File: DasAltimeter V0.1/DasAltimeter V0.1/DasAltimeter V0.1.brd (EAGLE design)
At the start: 39.6 x 21.8 mm, 57 parts, among them IC1 BMI055, U1 ATSAMD21G-A, U2 3.3V/150mA, U3 MS5803-14BA, U4 ADXL193, X1 22-23-2041, X2 22-23-2041, Y1 32.768kHz

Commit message: V0.1 board
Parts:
- removed C6: 0.1uF, SparkFun-Capacitors:0402
- moved C12 1.53 mm to (17.3, 5.46), turned to 0 degrees
- moved L1 0.89 mm to (20.3, 2.03)
- moved R23 0.40 mm to (31.2, 2.16)
- moved C10 0.38 mm to (31.2, 3.56)
- moved C11 0.38 mm to (24.6, 2.16)
- moved C8 0.38 mm to (34.4, 15.2)
- moved MEM 0.38 mm to (30.6, 17.7)
- moved R5 0.38 mm to (34.4, 20.1)
- moved R24 0.38 mm to (24.6, 3.56)
- moved R1 0.28 mm to (27.6, 17.4)
- moved D2 0.25 mm to (38.1, 9.53)
- moved R2 0.25 mm to (38.1, 9.53)
- moved U3 0.25 mm to (32.6, 8.89)
- moved R16 0.25 mm to (8.00, 13.1)
- moved R20 0.25 mm to (13.5, 13.1)
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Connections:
- removed net N$11: U1.33
- removed net N$14: U1.34
- removed net RESET: R1.1, U1.40
- new net RX: JP1.6, U1.32
- new net TX: JP1.8, U1.31
- net !RESET: now also R1.1, U1.40
- net 3.3V: no longer C6.1
- net BUZZER: now also U1.30; no longer U1.31
- net CS_ACCEL: now also U1.19; no longer U1.15
- net CS_BARO: now also U1.24; no longer U1.23
- net CS_GYRO: now also U1.15; no longer U1.19
- net FIRE_A: now also U1.38
- net FIRE_B: now also U1.37
- net FIRE_C: now also U1.34
- net FIRE_D: now also U1.33
- net GND: now also U1.18, U1.35, U1.42, U1.5; no longer C6.2
- net LED: now also U1.29
- net SENSE_A: now also U1.48; no longer U1.47
- net SENSE_B: now also U1.47; no longer U1.48
- net SPI2_MISO: now also U1.22; no longer U1.24
- net SPI2_SCK: now also U1.23; no longer U1.22
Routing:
- net VCC: track 0.00 -> 58.2 mm, vias 0 -> 3
- net 3.3V: track 0.00 -> 32.2 mm, vias 0 -> 14
- net FIRE_D: track 0.00 -> 24.6 mm, vias 0 -> 2
- net GND: track 0.00 -> 22.3 mm, vias 0 -> 24
- net FIRE_A: track 0.00 -> 20.3 mm, vias 0 -> 2
- net SENSE_D: track 0.00 -> 17.5 mm, vias 0 -> 2
- net FIRE_C: track 0.00 -> 17.4 mm
- net LED: track 0.00 -> 16.9 mm, vias 0 -> 1
- net SENSE_A: track 0.00 -> 15.3 mm, vias 0 -> 2
- net FIRE_B: track 0.00 -> 13.9 mm, vias 0 -> 2
- net CS_MEM: track 0.00 -> 12.5 mm
- net CS_BARO: track 0.00 -> 11.7 mm, vias 0 -> 2
- net SENSE_C: track 0.00 -> 11.6 mm, vias 0 -> 2
- net !RESET: track 0.00 -> 11.2 mm, vias 0 -> 1
- net SPI0_MISO: track 0.00 -> 11.1 mm
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- added copper zone on layer 15, net 3.3V
- added copper zone on layer 1, net GND
- added copper zone on layer 16, net GND
- added copper zone on layer 2, net GND

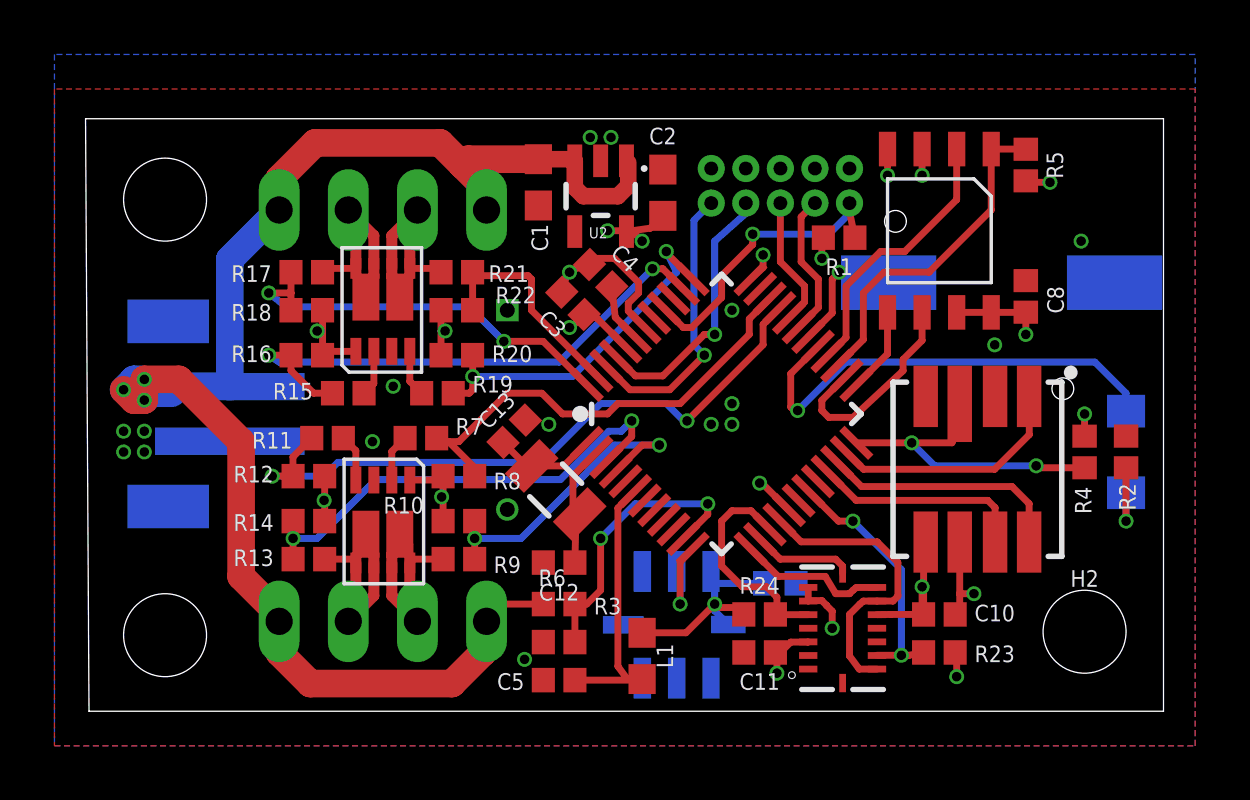
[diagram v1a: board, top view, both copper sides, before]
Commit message: DasAltimeter V0.1 sent to fab
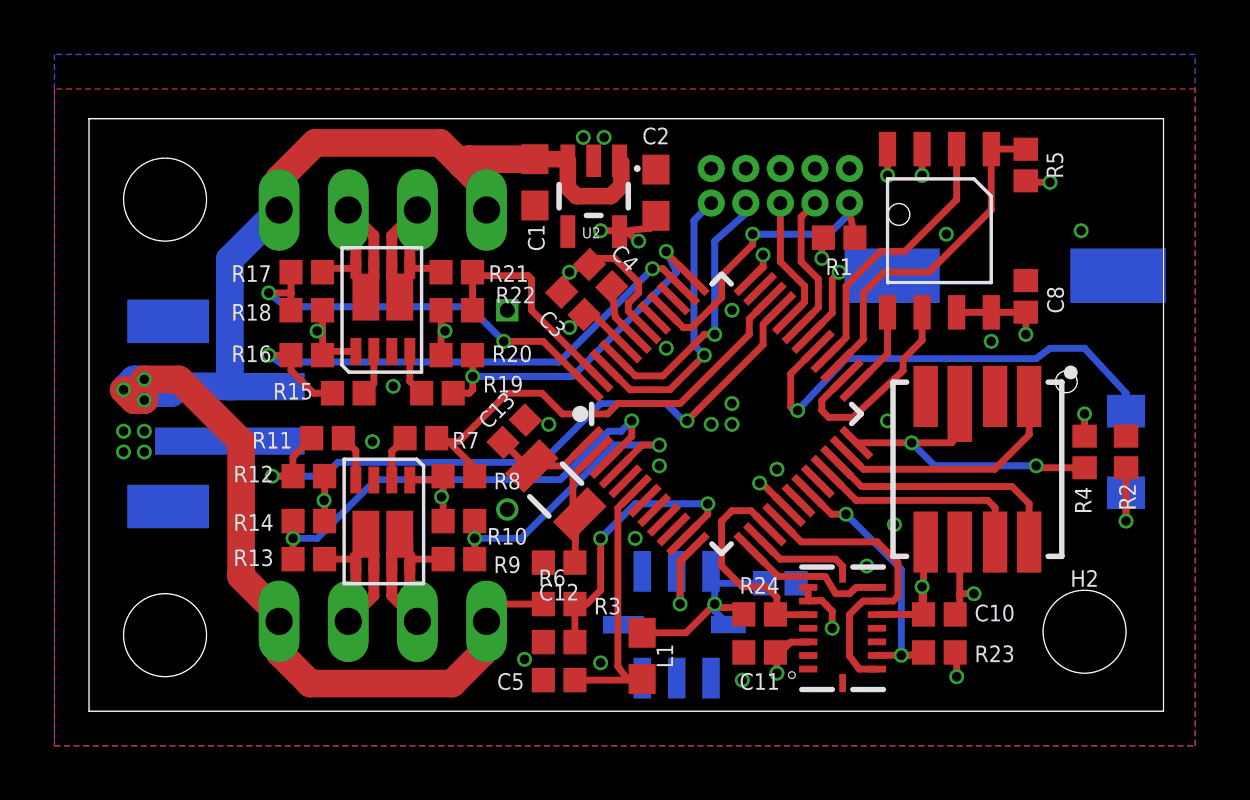
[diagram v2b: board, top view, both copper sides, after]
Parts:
- moved SG1 0.28 mm to (33.7, 16.0)
- moved C2 0.25 mm to (20.8, 19.1)
- moved U2 0.25 mm to (18.5, 18.9)
- moved C1 0.13 mm to (16.4, 19.4)
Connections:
- removed net N$9: U1.41
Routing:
- net GND: vias 24 -> 34
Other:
- board size 39.6 x 21.8 mm -> 39.5 x 21.8 mm
- board text added: "DasAltimeter"

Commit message: setting up software
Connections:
- net CS_BARO: now also U1.23; no longer U1.24
- net SPI2_SCK: now also U1.24; no longer U1.23
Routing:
- net CS_BARO: track 11.7 -> 19.0 mm
- net SPI2_SCK: track 8.90 -> 8.27 mm
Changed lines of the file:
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@@
 <via x="29.591" y="6.858" extent="1-16" drill="0.35"/>
 <via x="31.496" y="17.526" extent="1-16" drill="0.35"/>
-<via x="29.337" y="10.668" extent="1-16" drill="0.35"/>
+<via x="29.718" y="11.303" extent="1-16" drill="0.35"/>
 <via x="28.575" y="5.334" extent="1-16" drill="0.35"/>
 <via x="18.796" y="1.778" extent="1-16" drill="0.35"/>
@@
 <via x="34.417" y="13.843" extent="1-16" drill="0.35"/>
 <via x="22.987" y="3.937" extent="1-16" drill="0.35"/>
-<via x="25.273" y="1.397" extent="1-16" drill="0.35"/>
+<via x="25.273" y="1.27" extent="1-16" drill="0.35"/>
 <via x="30.607" y="4.572" extent="1-16" drill="0.35"/>
-<via x="36.576" y="10.922" extent="1-16" drill="0.35"/>
+<via x="36.576" y="11.049" extent="1-16" drill="0.35"/>
 <via x="24.638" y="8.382" extent="1-16" drill="0.35"/>
 <via x="26.924" y="16.637" extent="1-16" drill="0.35"/>
@@
 <wire x1="34.417" y1="13.843" x2="34.417" y2="14.526" width="0.254" layer="1"/>
 <wire x1="34.417" y1="14.526" x2="34.29" y2="14.653" width="0.254" layer="1"/>
-<wire x1="36.576" y1="10.922" x2="36.576" y2="10.105" width="0.254" layer="1"/>
+<wire x1="36.576" y1="11.049" x2="36.576" y2="10.105" width="0.254" layer="1"/>
 <via x="31.877" y="1.27" extent="1-16" drill="0.35"/>
 <wire x1="31.822" y1="2.159" x2="31.877" y2="2.104" width="0.254" layer="1"/>
 <wire x1="31.877" y1="2.104" x2="31.877" y2="1.27" width="0.254" layer="1"/>
 <wire x1="25.218" y1="2.159" x2="25.273" y2="2.104" width="0.254" layer="1"/>
-<wire x1="25.273" y1="2.104" x2="25.273" y2="1.397" width="0.254" layer="1"/>
+<wire x1="25.273" y1="2.104" x2="25.273" y2="1.27" width="0.254" layer="1"/>
 <wire x1="22.85" y1="5.135" x2="22.987" y2="4.998" width="0.254" layer="16"/>
 <wire x1="22.987" y1="4.699" x2="22.987" y2="3.937" width="0.254" layer="16"/>
@@
 <signal name="SPI2_SCK">
 <contactref element="U3" pad="1"/>
-<contactref element="U1" pad="23"/>
-<wire x1="27.83719375" y1="9.507784375" x2="28.454978125" y2="8.89" width="0.254" layer="1"/>
-<wire x1="33.274" y1="8.89" x2="34.544" y2="10.16" width="0.254" layer="1"/>
 <wire x1="34.544" y1="10.16" x2="34.544" y2="11.56" width="0.254" layer="1"/>
 <wire x1="34.544" y1="11.56" x2="34.539" y2="11.565" width="0.254" layer="1"/>
-<wire x1="28.454978125" y1="8.89" x2="33.274" y2="8.89" width="0.254" layer="1"/>
+<contactref element="U1" pad="24"/>
+<wire x1="28.190746875" y1="9.8613375" x2="28.7466625" y2="9.8613375" width="0.254" layer="1"/>
+<wire x1="28.7466625" y1="9.8613375" x2="29.21" y2="9.398" width="0.254" layer="1"/>
+<wire x1="29.21" y1="9.398" x2="33.782" y2="9.398" width="0.254" layer="1"/>
+<wire x1="33.782" y1="9.398" x2="34.544" y2="10.16" width="0.254" layer="1"/>
 </signal>
 <signal name="CS_BARO">
 <contactref element="U3" pad="3"/>
 <contactref element="R4" pad="1"/>
-<contactref element="U1" pad="24"/>
-<wire x1="28.190746875" y1="9.8613375" x2="30.226" y2="9.8613375" width="0.254" layer="1"/>
-<wire x1="30.226" y1="9.8613375" x2="31.7053375" y2="9.8613375" width="0.254" layer="1"/>
-<wire x1="31.7053375" y1="9.8613375" x2="31.877" y2="10.287" width="0.254" layer="1"/>
+<wire x1="29.337" y1="10.3693375" x2="29.337" y2="10.287" width="0.254" layer="1"/>
+<wire x1="29.337" y1="10.287" x2="29.845" y2="9.906" width="0.254" layer="1"/>
 <wire x1="31.877" y1="10.287" x2="31.877" y2="11.148" width="0.254" layer="1"/>
 <wire x1="31.877" y1="11.148" x2="31.989" y2="11.29" width="0.254" layer="1"/>
-<wire x1="36.576" y1="8.945" x2="34.87" y2="8.945" width="0.254" layer="1"/>
+<wire x1="34.87" y1="8.945" x2="36.576" y2="8.945" width="0.254" layer="1"/>
 <wire x1="34.87" y1="8.945" x2="34.798" y2="9.017" width="0.254" layer="1"/>
 <via x="34.798" y="9.017" extent="1-16" drill="0.35"/>
 <wire x1="34.798" y1="9.017" x2="31.0703375" y2="9.017" width="0.254" layer="16"/>
-<wire x1="31.0703375" y1="9.017" x2="30.226" y2="9.8613375" width="0.254" layer="16"/>
-<via x="30.226" y="9.8613375" extent="1-16" drill="0.35"/>
+<wire x1="31.0703375" y1="9.017" x2="29.337" y2="10.3693375" width="0.254" layer="16"/>
+<via x="29.337" y="10.3693375" extent="1-16" drill="0.35"/>
+<contactref element="U1" pad="23"/>
+<wire x1="27.83719375" y1="9.507784375" x2="28.454978125" y2="8.89" width="0.254" layer="1"/>
+<wire x1="34.815" y1="8.89" x2="34.87" y2="8.945" width="0.254" layer="1"/>
+<wire x1="28.454978125" y1="8.89" x2="34.815" y2="8.89" width="0.254" layer="1"/>
+<wire x1="29.845" y1="9.906" x2="31.496" y2="9.906" width="0.254" layer="1"/>
+<wire x1="31.496" y1="9.906" x2="31.877" y2="10.287" width="0.254" layer="1"/>
 </signal>
 <signal name="ACCELX">
